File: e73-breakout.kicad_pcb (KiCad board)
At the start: 2 copper layers, 25.4 x 33 mm, 16 parts, among them J1 Conn_ARM_JTAG_SWD_10, J2 Pin, J3 Pin, J4 Pin, SW1 SW_Push, U1 E73-2G4M04S-52810

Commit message: symbols
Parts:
- added REF**: SymbolLeadFree, e73-breakout:SymbolLeadFree, B.Cu at (100.0, 89.8)
- added REF**: SymbolIdDots, e73-breakout:SymbolIdDots, B.Cu at (100.0, 93.7)
- added SW2: 3x4mm, Button_Switch_SMD:SW_Push_SPST_NO_Alps_SKRK, F.Cu at (108.3, 116.5)
- SW1: value SW_Push -> 2x3mm
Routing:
- net GND: track 19.4 -> 23.5 mm
- net /NFC1: track 18.5 -> 19.0 mm

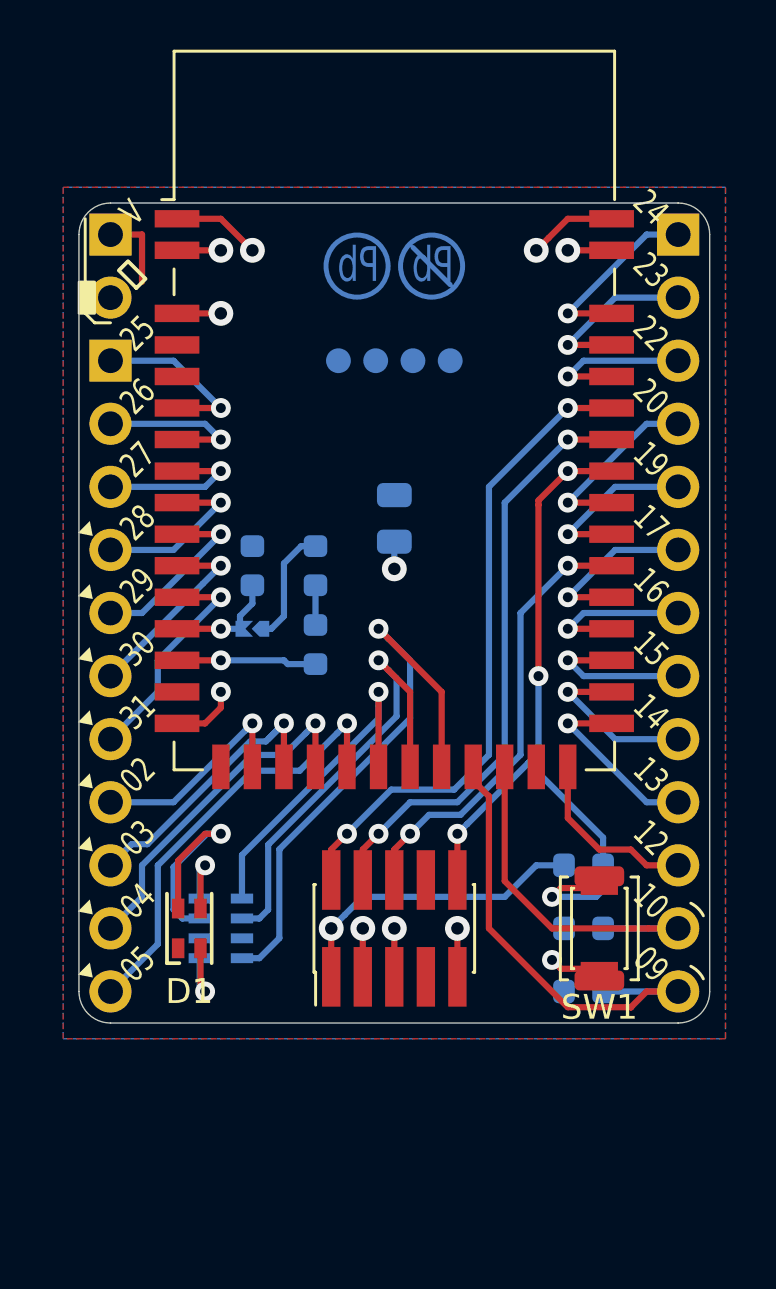
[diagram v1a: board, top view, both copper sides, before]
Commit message: Move switch off reset, add silk rev
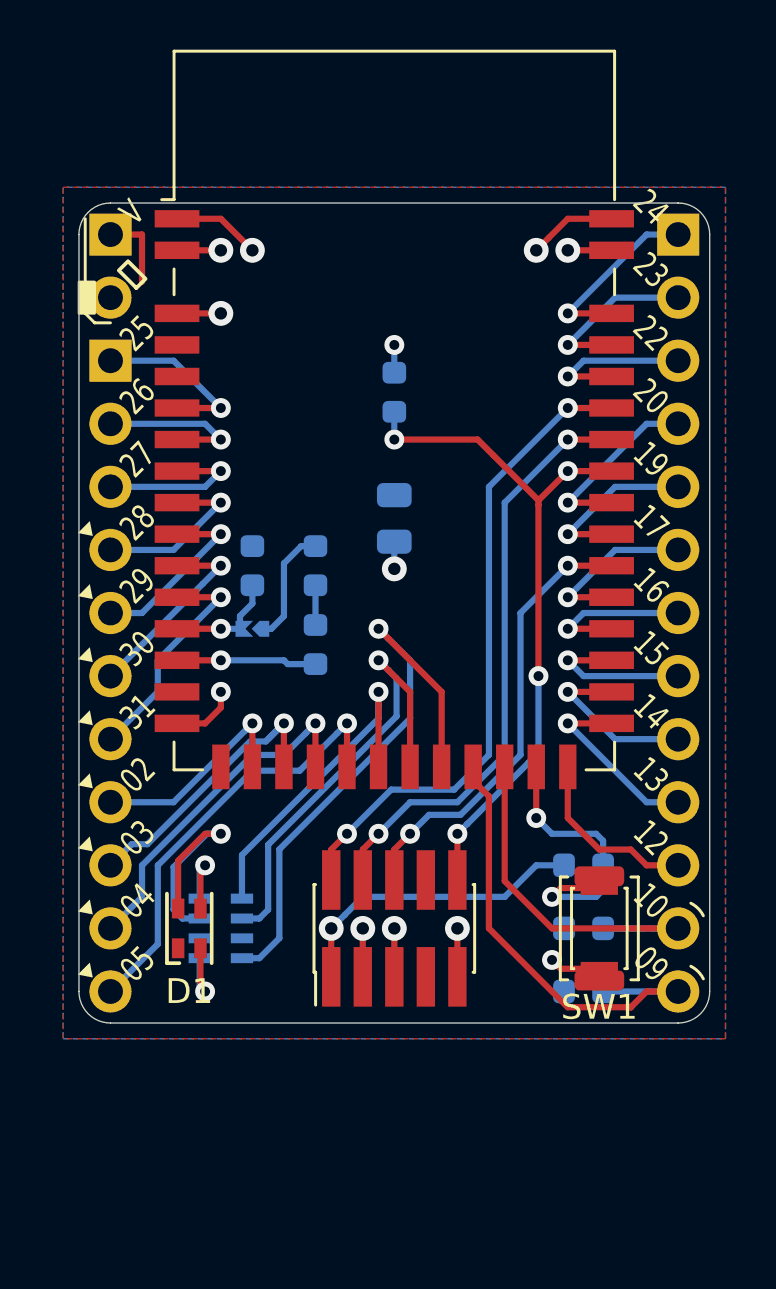
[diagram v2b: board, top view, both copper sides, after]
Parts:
- removed REF**: SymbolLeadFree, e73-breakout:SymbolLeadFree
- removed REF**: SymbolIdDots, e73-breakout:SymbolIdDots
- added R2: 10k, Resistor_SMD:R_0603_1608Metric, B.Cu at (100.0, 94.9)
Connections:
- R1 pad 2: /~RST -> /SW
- SW1 pad 1: /~RST -> /SW
- SW2 pad 1: /~RST -> /SW
- U1 pad 26: (no net) -> /SW
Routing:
- net /SW: track 0.00 -> 11.8 mm, vias 0 -> 2
- net /~RST: track 31.1 -> 28.0 mm
- net +3V3: track 16.6 -> 17.8 mm, vias 2 -> 3
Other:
- net class Default: clearance 0.2 -> 0.1524
- net class Thick: clearance 0.2 -> 0.1524
- rule trace_clearance: 0.2 -> 0.1524
- rule trace_min: 0.2 -> 0.1524
- board text added: "E73-2G4M04S1(A/B/D) Breakout v1"

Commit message: not actually D compatible; generate gerbers
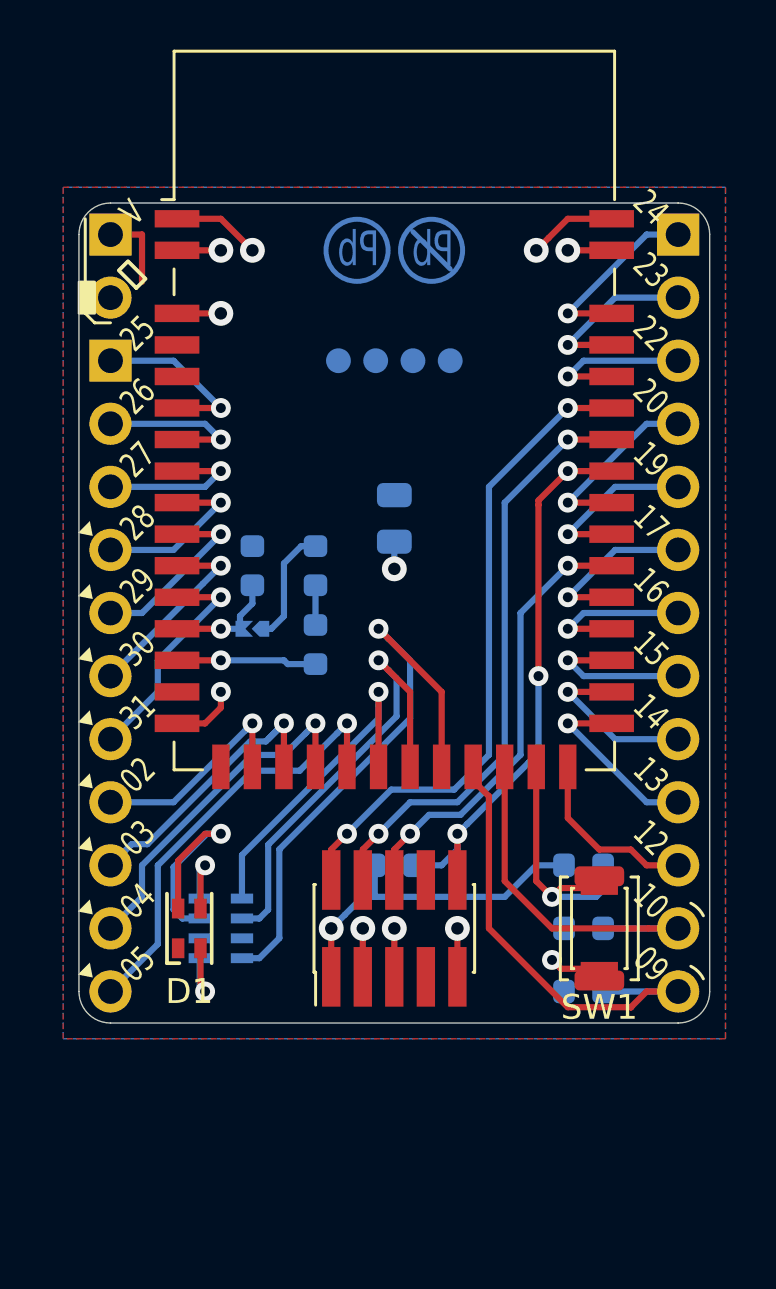
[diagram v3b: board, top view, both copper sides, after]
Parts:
- added H1: Symbol, e73-breakout:SymbolLeadFree, B.Cu at (100.0, 89.2)
- added H2: Symbol, e73-breakout:SymbolIdDots, B.Cu at (100.0, 93.7)
- moved R2 19.0 mm to (100.0, 114.0), turned to 0 degrees
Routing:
- net /~RST: track 28.0 -> 22.7 mm, vias 4 -> 3
- net /SW: track 11.8 -> 11.2 mm, vias 2 -> 1
- net +3V3: track 17.8 -> 17.9 mm, vias 3 -> 2
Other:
- board text added: "E73-2G4M04S1(A/B) Breakout v1"
- board text removed: "E73-2G4M04S1(A/B/D) Breakout v1"

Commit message: Forking the original repo to make a D compatible breakout.
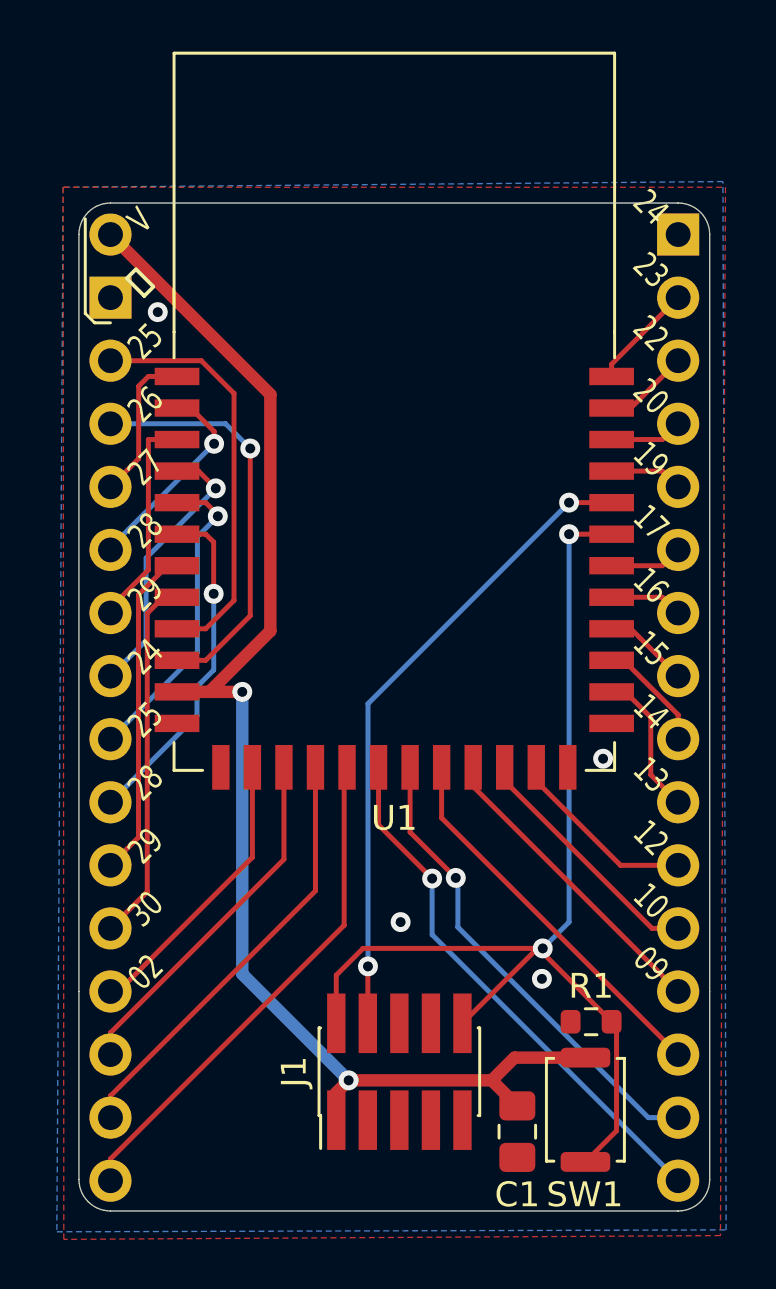
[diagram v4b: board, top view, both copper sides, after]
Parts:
- removed C2: 1uF, Capacitor_SMD:C_0603_1608Metric
- removed C4, C5: 4pF, Capacitor_SMD:C_0603_1608Metric
- removed D1: LED_ARGB, e73-breakout:LED_RGB_0606
- removed H1: Symbol, e73-breakout:SymbolLeadFree
- removed H2: Symbol, e73-breakout:SymbolIdDots
- removed JP1: SolderJumper_2_Open, e73-breakout:SolderJumper-0402
- removed L1: 10uH, Inductor_SMD:L_0603_1608Metric
- removed L2: 15nH, Inductor_SMD:L_0603_1608Metric
- removed R2: 10k, Resistor_SMD:R_0603_1608Metric
- removed RN1: 1k, Resistor_SMD:R_Array_Concave_4x0603
- removed SW2: 3x4mm, Button_Switch_SMD:SW_Push_SPST_NO_Alps_SKRK
- C1: footprint Capacitor_SMD:C_0805_2012Metric -> Capacitor_SMD:C_0805_2012Metric_Pad1.18x1.45mm_HandSolder; moved to F.Cu
- J3: footprint Connector_PinHeader_2.54mm:PinHeader_1x13_P2.54mm_Vertical -> Connector_PinHeader_2.54mm:PinHeader_1x16_P2.54mm_Vertical
- J4: footprint Connector_PinHeader_2.54mm:PinHeader_1x11_P2.54mm_Vertical -> Connector_PinHeader_2.54mm:PinHeader_1x14_P2.54mm_Vertical
- R1: moved to F.Cu
- SW1: footprint Button_Switch_SMD:SW_SPST_CK_KXT3 -> Button_Switch_SMD:SW_Push_SPST_NO_Alps_SKRK
- U1: value E73-2G4M04S-52810 -> E73-2G4M04S1D-51822; footprint RF_Module:E73-2G4M04S -> RF_Module:E73-2G4M04S1D
- moved C1 25.2 mm to (105.0, 124.7), turned to -90 degrees
- moved SW1 7.32 mm to (107.7, 123.8), turned to 90 degrees
- moved R1 6.31 mm to (107.9, 120.3)
- moved J1 5.77 mm to (100.2, 122.3)
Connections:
- J1 pad 10: /~RST -> /SWDIO
- J1 pad 7: (no net) -> unconnected-(J1-KEY-Pad7)
- J1 pad 8: (no net) -> unconnected-(J1-NC/TDI-Pad8)
- J3 pad 1: /R1 -> GND
- J3 pad 10: /R10 -> /P012
- J3 pad 11: /R11 -> /P011
- J3 pad 12: /NFC2 -> /P010
- J3 pad 13: /NFC1 -> /P009
- J3 pad 2: /R2 -> /P020
- J3 pad 3: /R3 -> /P019
- J3 pad 4: /R4 -> /P018
- J3 pad 5: /R5 -> /P017
- J3 pad 6: /R6 -> /P016
- J3 pad 7: /R7 -> /P015
- J3 pad 8: /R8 -> /P014
- J3 pad 9: /R9 -> /P013
- J4 pad 1: /L3 -> /P000
- J4 pad 10: /L12 -> /P030
- J4 pad 11: /L13 -> /P002
- J4 pad 2: /L4 -> /P001
- J4 pad 3: /L5 -> /P021
- J4 pad 4: /L6 -> /P022
- J4 pad 5: /L7 -> /P023
- J4 pad 6: /L8 -> /P024
- J4 pad 7: /L9 -> /P025
- J4 pad 8: /L10 -> /P028
- J4 pad 9: /L11 -> /P029
- R1 pad 1: +3V3 -> GND
- R1 pad 2: /SW -> /SWDIO
- SW1 pad 1: /SW -> /SWDIO
- SW1 pad 2: GND -> +3V3
- U1 pad 1: GND -> /P021
- U1 pad 10: /L8 -> /P001
- U1 pad 11: /L9 -> +3V3
- U1 pad 12: /DEC4 -> GND
- U1 pad 13: /DCC -> GND
- U1 pad 14: (no net) -> /P002
- U1 pad 15: GND -> /P003
- U1 pad 16: +3V3 -> /P004
- U1 pad 17: /L10 -> /P005
- U1 pad 18: /L11 -> /P006
- U1 pad 19: /L12 -> /P007
- U1 pad 2: GND -> /P022
- U1 pad 20: /L13 -> /P008
- U1 pad 21: /RGB1 -> /P009
- U1 pad 22: /RGB2 -> /P010
- U1 pad 23: /RGB3 -> /P011
- U1 pad 24: /NFC1 -> GND
- U1 pad 25: /NFC2 -> GND
- U1 pad 26: /SW -> /P012
- U1 pad 27: /R11 -> /P013
- U1 pad 28: /R10 -> /P014
- U1 pad 29: /R9 -> /P015
- U1 pad 3: (no net) -> /P023
- U1 pad 30: /R8 -> /P016
- U1 pad 31: /R7 -> /SWDIO
- U1 pad 32: /R6 -> /SWDCLK
- U1 pad 33: /SWO -> /P017
- U1 pad 34: /R5 -> /P018
- U1 pad 35: /R4 -> /P019
- U1 pad 36: /~RST -> /P020
- U1 pad 4: (no net) -> /P024
- U1 pad 5: /L3 -> /P025
- U1 pad 6: /L4 -> /P028
- U1 pad 7: /L5 -> /P029
- U1 pad 8: /L6 -> /P030
- U1 pad 9: /L7 -> /P000
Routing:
- net +3V3: track 17.9 -> 55.3 mm
- net /RGB3: track 23.6 -> 0.00 mm, vias 1 -> 0
- net GND: track 23.5 -> 0.00 mm, vias 10 -> 4
- net /~RST: track 22.7 -> 0.00 mm, vias 3 -> 0
- net /P006: track 0.00 -> 21.6 mm, vias 0 -> 1
- net /P005: track 0.00 -> 20.6 mm
- net /P007: track 0.00 -> 19.3 mm, vias 0 -> 1
- net /NFC1: track 19.0 -> 0.00 mm
- net /SWO: track 18.9 -> 0.00 mm, vias 2 -> 0
- net /RGB2: track 18.5 -> 0.00 mm, vias 1 -> 0
- net /L13: track 17.6 -> 0.00 mm, vias 1 -> 0
- net /P004: track 0.00 -> 17.5 mm
- net /SWDIO: track 27.0 -> 44.4 mm
- net /P000: track 0.00 -> 16.6 mm
- net /P001: track 0.00 -> 16.5 mm, vias 0 -> 1
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- added copper zone on F.Cu, net GND
- removed copper zone on F.Cu, net +3V3
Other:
- board size 25.4 x 33 mm -> 25.4 x 40.6 mm
- net class Default removed
- net class Thick removed
- net class Thin removed
- board text added: "E73-2G4M04S1D Breakout v1"
- board text removed: "03"
- board text removed: "04"
- board text removed: "05"
- board text removed: "31"
- board text removed: "E73-2G4M04S1(A/B) Breakout v1"
- board text removed: "▸"

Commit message: Some updates and pictures.
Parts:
- C1: footprint Capacitor_SMD:C_0805_2012Metric_Pad1.18x1.45mm_HandSolder -> Capacitor_THT:C_Disc_D3.0mm_W1.6mm_P2.50mm
- J1: footprint Connector_PinHeader_1.27mm:PinHeader_2x05_P1.27mm_Vertical_SMD -> Connector_PinHeader_1.27mm:PinHeader_2x05_P1.27mm_Vertical
- R1: footprint Resistor_SMD:R_0603_1608Metric -> Resistor_THT:R_Axial_DIN0204_L3.6mm_D1.6mm_P5.08mm_Horizontal
- SW1: footprint Button_Switch_SMD:SW_Push_SPST_NO_Alps_SKRK -> kbd:ResetSW_1side
- moved R1 14.2 mm to (94.8, 125.6), turned to 90 degrees
- moved J1 4.01 mm to (97.2, 125.0)
- moved C1 1.69 mm to (104.7, 123.0)
- moved SW1 0.47 mm to (107.7, 123.3)
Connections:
- J1 pad 6: /SWO -> unconnected-(J1-SWO/TDO-Pad6)
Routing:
- net +3V3: track 55.3 -> 60.1 mm, vias 2 -> 1
- net /SWDIO: track 44.4 -> 40.1 mm
- net /SWDCLK: track 26.0 -> 29.6 mm, vias 2 -> 1
- net /P009: track 12.4 -> 13.1 mm
- net GND: vias 4 -> 3
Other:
- board text added: "E73-2G4M04S1D-51822 Breakout v0.1"
- board text removed: "E73-2G4M04S1D Breakout v1"
